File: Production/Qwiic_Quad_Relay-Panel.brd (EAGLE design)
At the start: 96.3 x 222.2 mm, 517 parts, among them J10 Qwiic Right Angle, J11 Qwiic Right Angle, J12 AVR_SPI_PROG_3X2TESTPOINTS, J18 POWER_JACK, J19 Qwiic Right Angle, J2 Qwiic Right Angle, J20 Qwiic Right Angle, J21 AVR_SPI_PROG_3X2TESTPOINTS, J27 POWER_JACK, J28 Qwiic Right Angle, J29 Qwiic Right Angle, J3 Qwiic Right Angle, J30 AVR_SPI_PROG_3X2TESTPOINTS, J36 POWER_JACK, J4 POWER_JACK, J9 AVR_SPI_PROG_3X2TESTPOINTS, K1 RELAY-SPDT-JZC-11F, K10 RELAY-SPDT-JZC-11F, K11 RELAY-SPDT-JZC-11F, K12 RELAY-SPDT-JZC-11F, K13 RELAY-SPDT-JZC-11F, K14 RELAY-SPDT-JZC-11F, K15 RELAY-SPDT-JZC-11F, K16 RELAY-SPDT-JZC-11F, K2 RELAY-SPDT-JZC-11F, K3 RELAY-SPDT-JZC-11F, K4 RELAY-SPDT-JZC-11F, K5 RELAY-SPDT-JZC-11F, K6 RELAY-SPDT-JZC-11F, K7 RELAY-SPDT-JZC-11F, K8 RELAY-SPDT-JZC-11F, K9 RELAY-SPDT-JZC-11F, Q1 600mA/40V, Q10 600mA/40V, Q11 600mA/40V, Q12 600mA/40V, Q13 600mA/40V, Q14 600mA/40V, Q15 600mA/40V, Q16 600mA/40V, Q2 600mA/40V, Q3 600mA/40V, Q4 600mA/40V, Q5 600mA/40V, Q6 600mA/40V, Q7 600mA/40V, Q8 600mA/40V, Q9 600mA/40V, U1 LMR14010A, U10 DUAL-OPTOISOLATOR_SOIC8, U11 ATTINY84-ARDUINO, U12 LMR14010A, U13 DUAL-OPTOISOLATOR_SOIC8, U14 DUAL-OPTOISOLATOR_SOIC8, U15 ATTINY84-ARDUINO, U16 LMR14010A, U2 DUAL-OPTOISOLATOR_SOIC8, U3 DUAL-OPTOISOLATOR_SOIC8, U4 ATTINY84-ARDUINO, U5 DUAL-OPTOISOLATOR_SOIC8, U6 DUAL-OPTOISOLATOR_SOIC8, U7 ATTINY84-ARDUINO, U8 LMR14010A, U9 DUAL-OPTOISOLATOR_SOIC8

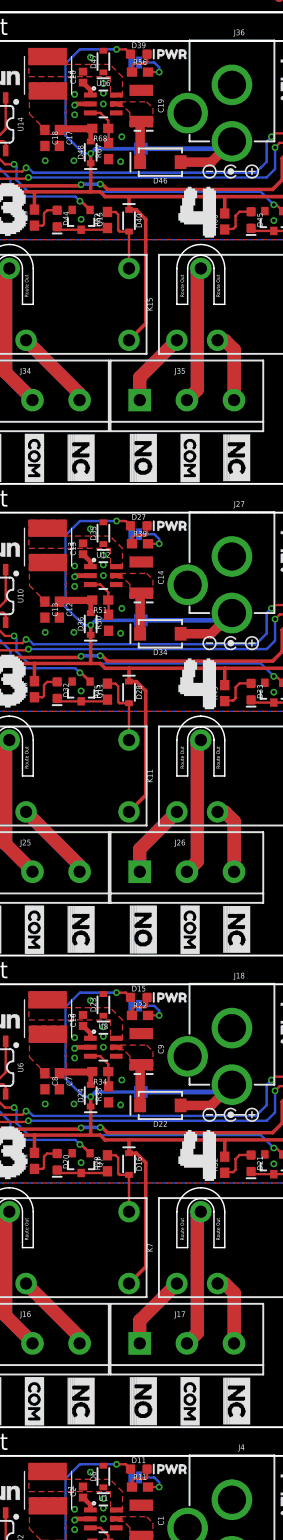
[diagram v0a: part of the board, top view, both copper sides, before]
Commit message: Updates production panel following latest commit
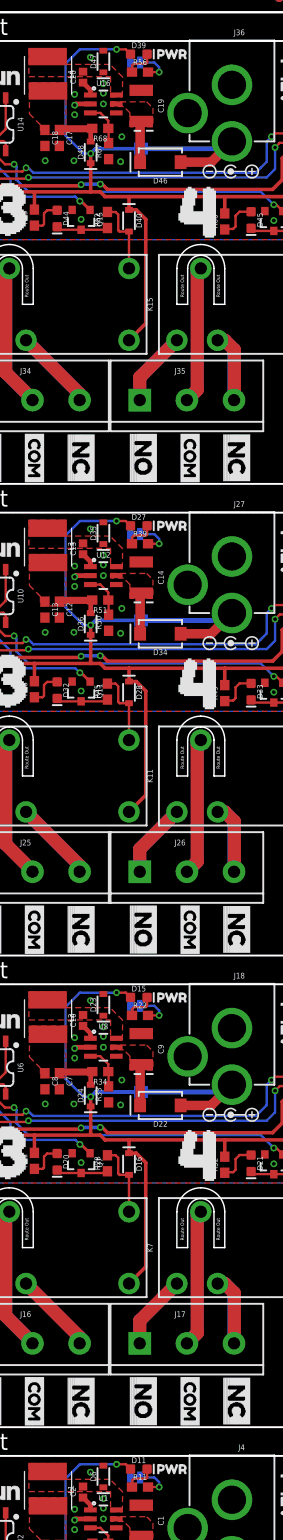
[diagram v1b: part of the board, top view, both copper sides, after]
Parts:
- LED, LED1, LED2, LED3: value JUMPER-SMT_2_NO_SILK -> JUMPER-SMT_2_NC_TRACE_SILK; device SparkFun-Jumpers:SMT-JUMPER_2_NO_SILK -> SparkFun-Jumpers:SMT-JUMPER_2_NC_TRACE_SILK

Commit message: Adds new production panel
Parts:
- added E$6: (no value), SparkFun-Retired:FIDUCIAL-1.5X3
- D23, D35, D47, D6: value 3A/10V/280mV -> 1A/23V/620mV
- R10, R18, R2, R27, R28, R29, R35, R4, R44, R45, R46, R52, R61, R62, R63, R8: value 33 -> 0
- moved E$5 14.5 mm to (-2.62, 6.35)
- moved E$3 10.7 mm to (85.2, 197.0)
- moved E$4 10.7 mm to (85.2, 197.0)
- moved E$1 10.6 mm to (-2.62, 197.0)
- moved E$2 10.6 mm to (-2.62, 197.0)
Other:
- board size 96.3 x 222.2 mm -> 96.3 x 218.9 mm
- board text added: "v21"
- board text removed: "v20"
